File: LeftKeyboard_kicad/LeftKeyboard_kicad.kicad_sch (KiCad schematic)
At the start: 45 parts, among them U1 Arduino_Pro_Micro

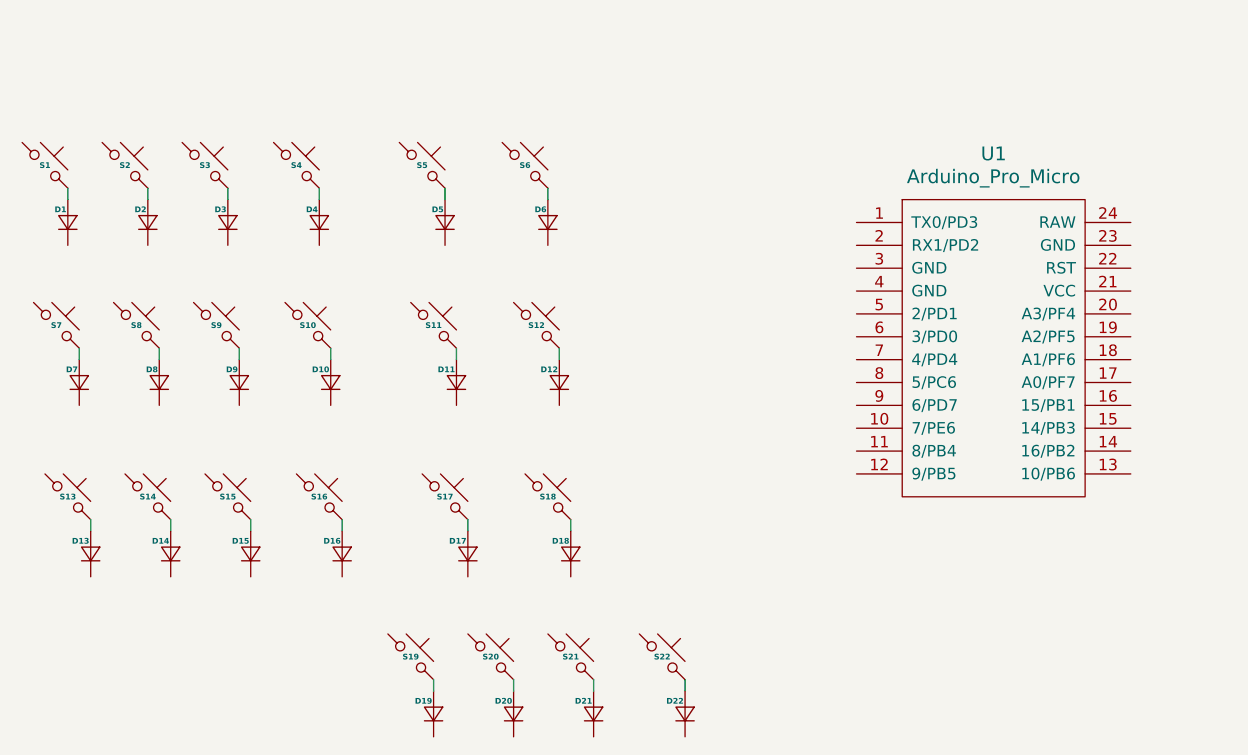
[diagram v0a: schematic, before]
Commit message: Completed schematic for left keyboard
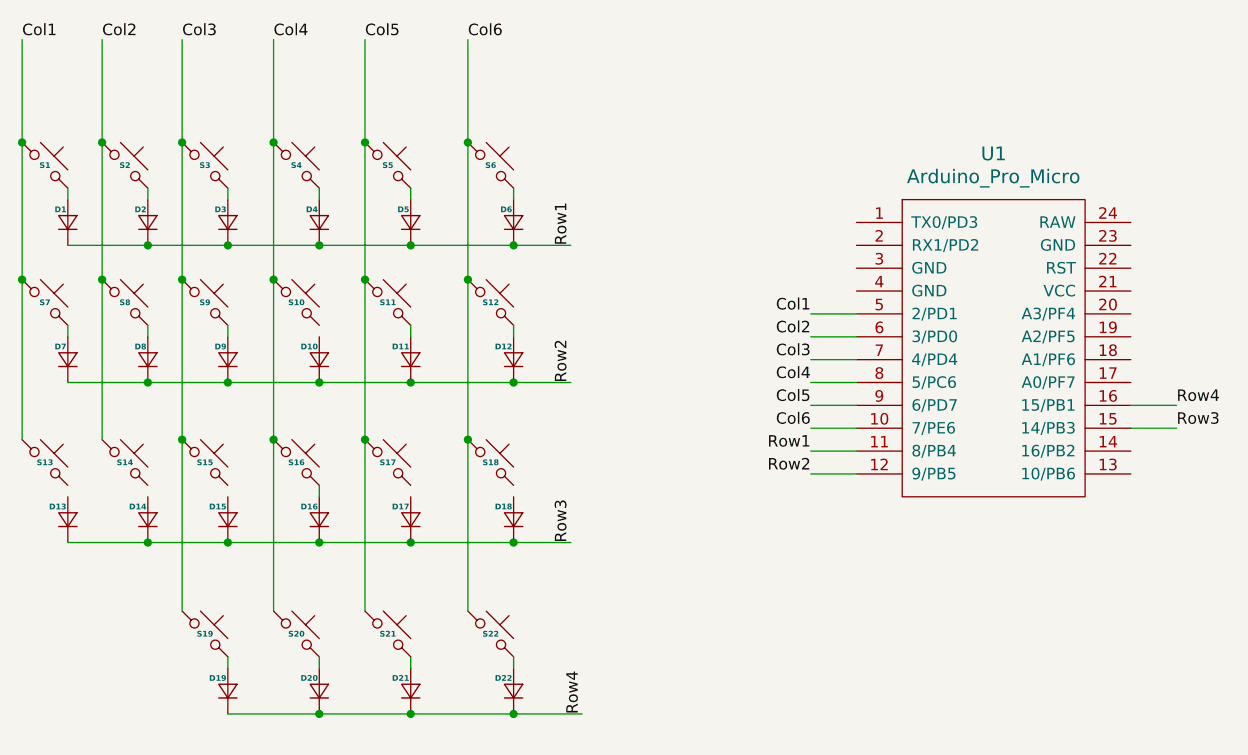
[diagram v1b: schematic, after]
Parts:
- D1, D10, D11, D12, D13, D14, D15, D16, D17, D18, D19, D2, D20, D21, D22, D3, D4, D5, D6, D7, D8, D9: footprint (none) -> ScottoKeebs_Components:Diode_DO-35
- S1, S13, S19, S20, S21, S7: footprint (none) -> ScottoKeebs_MX:MX_PCB_1.25u
- S10, S11, S12, S14, S15, S16, S17, S18, S2, S3, S4, S5, S6, S8, S9: footprint (none) -> ScottoKeebs_MX:MX_PCB_1.00u
- S22: footprint (none) -> ScottoKeebs_MX:MX_PCB_1.50u
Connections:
- net Row1: now reaches D2.1 (K)
- net Row1: now also D1.1 (K), D3.1 (K), D4.1 (K), D5.1 (K), D6.1 (K), U1.11 (8/PB4)
- net Col4: now reaches S10.1
- net Col4: now also S16.1, S20.1, S4.1, U1.8 (5/PC6)
- net at S10.2: no longer D10.2 (A)
- net Col6: now reaches S22.1
- net Col6: now also S12.1, S18.1, S6.1, U1.10 (7/PE6)
- net Row2: now reaches U1.12 (9/PB5)
- net Row2: now also D10.1 (K), D11.1 (K), D12.1 (K), D7.1 (K), D8.1 (K), D9.1 (K)
- net Row3: now reaches U1.15 (14/PB3)
- net Row3: now also D13.1 (K), D14.1 (K), D15.1 (K), D16.1 (K), D17.1 (K), D18.1 (K)
- net Row4: now reaches U1.16 (15/PB1)
- net Row4: now also D19.1 (K), D20.1 (K), D21.1 (K), D22.1 (K)
- net Col1: now reaches U1.5 (2/PD1)
- net Col1: now also S1.1, S13.1, S7.1
- net Col2: now reaches U1.6 (3/PD0)
- net Col2: now also S14.1, S2.1, S8.1
- net Col3: now reaches U1.7 (4/PD4)
- net Col3: now also S15.1, S19.1, S3.1, S9.1
- net Col5: now reaches U1.9 (6/PD7)
- net Col5: now also S11.1, S17.1, S21.1, S5.1
- net at D18.2 (A): no longer S18.2
- net at S14.2: no longer D14.2 (A)
- net at S15.2: no longer D15.2 (A)
- net at S17.2: no longer D17.2 (A)
- net at S13.2: no longer D13.2 (A)
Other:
- moved on the sheet: D10, D11, D12, D13, D14, D15, D16, D17, D18, D5, D6, D7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

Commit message: made considerable progress on pcb layout
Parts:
- D1, D10, D11, D12, D13, D14, D15, D16, D17, D18, D19, D2, D20, D21, D22, D3, D4, D5, D6, D7, D8, D9: footprint ScottoKeebs_Components:Diode_DO-35 -> ScottoKeebs_Components:Diode_SOD-123
- S19, S20, S21: footprint ScottoKeebs_MX:MX_PCB_1.25u -> ScottoKeebs_MX:MX_PCB_1.00u
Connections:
- net at S10.2: now also D10.2 (A)
- net at D18.2 (A): now also S18.2
- net at S14.2: now also D14.2 (A)
- net at S15.2: now also D15.2 (A)
- net at S17.2: now also D17.2 (A)
- net at S13.2: now also D13.2 (A)
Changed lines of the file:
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@@
 	(wire
 		(pts
+			(xy 76.2 87.63) (xy 76.2 88.9)
+		)
+		(stroke
+			(width 0)
+			(type default)
+		)
+	)
+	(wire
+		(pts
 			(xy 158.75 76.2) (xy 163.83 76.2)
 		)
@@
 	(wire
 		(pts
+			(xy 104.14 69.85) (xy 104.14 71.12)
+		)
+		(stroke
+			(width 0)
+			(type default)
+		)
+	)
+	(wire
+		(pts
 			(xy 88.9 38.1) (xy 88.9 49.53)
 		)
@@
 	(wire
 		(pts
+			(xy 114.3 87.63) (xy 114.3 88.9)
+		)
+		(stroke
+			(width 0)
+			(type default)
+		)
+	)
+	(wire
+		(pts
 			(xy 104.14 54.61) (xy 104.14 55.88)
 		)
@@
 	(wire
 		(pts
+			(xy 93.98 87.63) (xy 93.98 88.9)
+		)
+		(stroke
+			(width 0)
+			(type default)
+		)
+	)
+	(wire
+		(pts
 			(xy 85.09 54.61) (xy 85.09 55.88)
 		)
@@
 	(wire
 		(pts
+			(xy 85.09 87.63) (xy 85.09 88.9)
+		)
+		(stroke
+			(width 0)
+			(type default)
+		)
+	)
+	(wire
+		(pts
 			(xy 125.73 113.03) (xy 133.35 113.03)
 		)
@@
 	(wire
 		(pts
+			(xy 125.73 87.63) (xy 125.73 88.9)
+		)
+		(stroke
+			(width 0)
+			(type default)
+		)
+	)
+	(wire
+		(pts
 			(xy 109.22 64.77) (xy 109.22 82.55)
 		)
@@
 			)
 		)
-		(property "Footprint" "ScottoKeebs_Components:Diode_DO-35"
+		(property "Footprint" "ScottoKeebs_Components:Diode_SOD-123"
 			(at 85.09 58.42 90)
 			(effects
@@
 			)
 		)
-		(property "Footprint" "ScottoKeebs_Components:Diode_DO-35"
+		(property "Footprint" "ScottoKeebs_Components:Diode_SOD-123"
 			(at 104.14 58.42 90)
 			(effects
@@
 			)
 		)
-		(property "Footprint" "ScottoKeebs_Components:Diode_DO-35"
+		(property "Footprint" "ScottoKeebs_Components:Diode_SOD-123"
 			(at 114.3 58.42 90)
 			(effects
@@
 			)
 		)
-		(property "Footprint" "ScottoKeebs_Components:Diode_DO-35"
+		(property "Footprint" "ScottoKeebs_Components:Diode_SOD-123"
 			(at 114.3 73.66 90)
 			(effects
@@
 			)
 		)
-		(property "Footprint" "ScottoKeebs_Components:Diode_DO-35"
+		(property "Footprint" "ScottoKeebs_Components:Diode_SOD-123"
 			(at 125.73 91.44 90)
 			(effects
@@
 			)
 		)
-		(property "Footprint" "ScottoKeebs_Components:Diode_DO-35"
+		(property "Footprint" "ScottoKeebs_Components:Diode_SOD-123"
 			(at 76.2 73.66 90)
 			(effects
@@
 			)
 		)
-		(property "Footprint" "ScottoKeebs_Components:Diode_DO-35"
+		(property "Footprint" "ScottoKeebs_Components:Diode_SOD-123"
 			(at 93.98 91.44 90)
 			(effects
@@
 			)
 		)
-		(property "Footprint" "ScottoKeebs_Components:Diode_DO-35"
+		(property "Footprint" "ScottoKeebs_Components:Diode_SOD-123"
 			(at 93.98 58.42 90)
 			(effects
@@
 			)
 		)
-		(property "Footprint" "ScottoKeebs_Components:Diode_DO-35"
+		(property "Footprint" "ScottoKeebs_Components:Diode_SOD-123"
 			(at 85.09 91.44 90)
 			(effects
@@
 			)
 		)
-		(property "Footprint" "ScottoKeebs_Components:Diode_DO-35"
+		(property "Footprint" "ScottoKeebs_Components:Diode_SOD-123"
 			(at 125.73 110.49 90)
 			(effects
@@
 			)
 		)
-		(property "Footprint" "ScottoKeebs_Components:Diode_DO-35"
+		(property "Footprint" "ScottoKeebs_Components:Diode_SOD-123"
 			(at 104.14 73.66 90)
 			(effects
@@
 			)
 		)
-		(property "Footprint" "ScottoKeebs_Components:Diode_DO-35"
+		(property "Footprint" "ScottoKeebs_Components:Diode_SOD-123"
 			(at 104.14 91.44 90)
 			(effects
@@
 			)
 		)
-		(property "Footprint" "ScottoKeebs_Components:Diode_DO-35"
+		(property "Footprint" "ScottoKeebs_Components:Diode_SOD-123"
 			(at 125.73 58.42 90)
 			(effects
@@
 			)
 		)
-		(property "Footprint" "ScottoKeebs_Components:Diode_DO-35"
+		(property "Footprint" "ScottoKeebs_Components:Diode_SOD-123"
 			(at 104.14 110.49 90)
 			(effects
@@
 			)
 		)
-		(property "Footprint" "ScottoKeebs_Components:Diode_DO-35"
+		(property "Footprint" "ScottoKeebs_Components:Diode_SOD-123"
 			(at 114.3 91.44 90)
 			(effects
@@
 			)
 		)
-		(property "Footprint" "ScottoKeebs_Components:Diode_DO-35"
+		(property "Footprint" "ScottoKeebs_Components:Diode_SOD-123"
 			(at 76.2 58.42 90)
 			(effects
@@
 			)
 		)
-		(property "Footprint" "ScottoKeebs_Components:Diode_DO-35"
+		(property "Footprint" "ScottoKeebs_Components:Diode_SOD-123"
 			(at 114.3 110.49 90)
 			(effects
@@
 			)
 		)
-		(property "Footprint" "ScottoKeebs_MX:MX_PCB_1.25u"
+		(property "Footprint" "ScottoKeebs_MX:MX_PCB_1.00u"
 			(at 101.6 104.14 0)
 			(effects
@@
 			)
 		)
-		(property "Footprint" "ScottoKeebs_MX:MX_PCB_1.25u"
+		(property "Footprint" "ScottoKeebs_MX:MX_PCB_1.00u"
 			(at 111.76 104.14 0)
 			(effects
@@
 			)
 		)
-		(property "Footprint" "ScottoKeebs_MX:MX_PCB_1.25u"
+		(property "Footprint" "ScottoKeebs_MX:MX_PCB_1.00u"
 			(at 91.44 104.14 0)
 			(effects
@@
 			)
 		)
-		(property "Footprint" "ScottoKeebs_Components:Diode_DO-35"
+		(property "Footprint" "ScottoKeebs_Components:Diode_SOD-123"
 			(at 93.98 73.66 90)
 			(effects
@@
 			)
 		)
-		(property "Footprint" "ScottoKeebs_Components:Diode_DO-35"
+		(property "Footprint" "ScottoKeebs_Components:Diode_SOD-123"
 			(at 76.2 91.44 90)
 			(effects
@@
 			)
 		)
-		(property "Footprint" "ScottoKeebs_Components:Diode_DO-35"
+		(property "Footprint" "ScottoKeebs_Components:Diode_SOD-123"
 			(at 85.09 73.66 90)
 			(effects
@@
 			)
 		)
-		(property "Footprint" "ScottoKeebs_Components:Diode_DO-35"
+		(property "Footprint" "ScottoKeebs_Components:Diode_SOD-123"
 			(at 93.98 110.49 90)
 			(effects
@@
 			)
 		)
-		(property "Footprint" "ScottoKeebs_Components:Diode_DO-35"
+		(property "Footprint" "ScottoKeebs_Components:Diode_SOD-123"
 			(at 125.73 73.66 90)
 			(effects

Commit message: finish Left PCB, starting right
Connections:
- net GND: now reaches U1.3 (GND)
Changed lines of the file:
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@@
+	(wire
+		(pts
+			(xy 158.75 63.5) (xy 163.83 63.5)
+		)
+		(stroke
+			(width 0)
+			(type default)
+		)
+	)
 	(wire
 		(pts
@@
 		)
 	)
+	(label "GND"
+		(at 158.75 63.5 180)
+		(effects
+			(font
+				(size 1.27 1.27)
+			)
+			(justify right bottom)
+		)
+	)
